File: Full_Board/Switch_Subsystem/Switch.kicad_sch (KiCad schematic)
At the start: 7 parts, among them U7 JS102011SCQN, U8 UCLAMP3301H.TCT

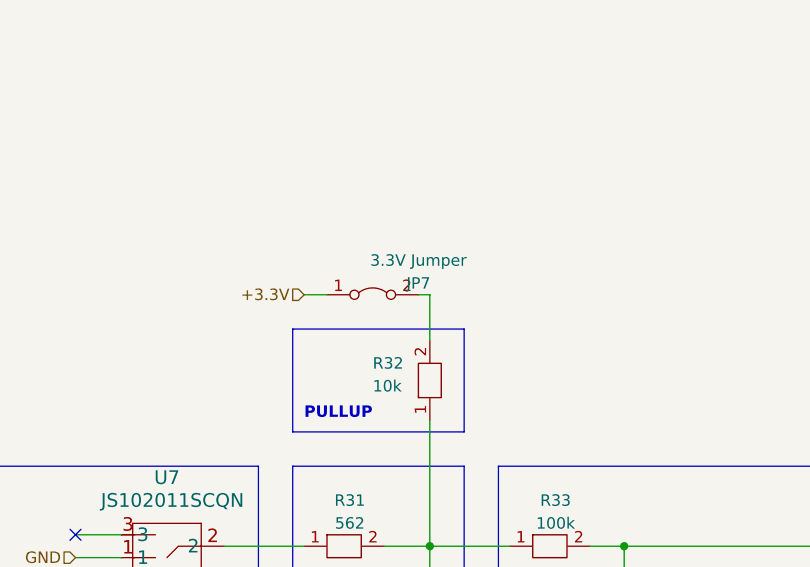
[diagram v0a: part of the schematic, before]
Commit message: Cleanup all schematics and project libs
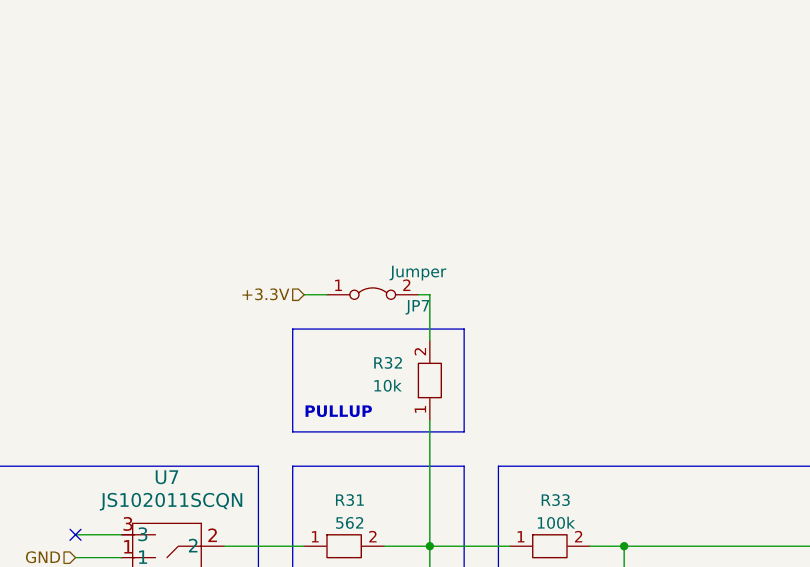
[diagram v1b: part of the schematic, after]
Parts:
- C17: Digikey Link (none) -> https://www.digikey.com/en/products/detail/kemet/C1210C822K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; Digikey link https://www.digikey.com/en/products/detail/kemet/C1210C822K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 -> (none); Mouser Link (none) -> https://www.mouser.com/ProductDetail/KEMET/C1210C822K2RACAU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; Mouser link https://www.mouser.com/ProductDetail/KEMET/C1210C822K2RACAU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 -> (none)
- JP7: value 3.3V Jumper -> Jumper; symbol Jumper:Jumper_2_Bridged -> PH1-02-UA:PH1-02-UA; Digikey Link https://www.digikey.com/en/products/detail/adam-tech/PH1-02-UA/9830266 -> https://www.digikey.com/en/products/detail/adam-tech/PH1-02-UA/9830266?s=N4IgTCBcDa4AwFYDsBaACgCQIwrmFAqgIIoByAIiALoC%2BQA; Manufacturer's Part Number (none) -> PH1-02-UA; Manufacturers Part Number PH1-02-UA -> (none)
- R31: Digikey Link (none) -> https://www.digikey.com/en/products/detail/bourns-inc/CR040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; Digikey link https://www.digikey.com/en/products/detail/bourns-inc/CR040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 -> (none); Mouse link https://www.mouser.com/ProductDetail/Bourns/CR0402-FX-5620G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 -> (none); Mouser Link (none) -> https://www.mouser.com/ProductDetail/Bourns/CR0402-FX-5620G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
- R32: Digikey Link (none) -> https://www.digikey.com/en/products/detail/stackpole-electr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; Digikey link https://www.digikey.com/en/products/detail/stackpole-electr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 -> (none)
- R33: Digikey Link (none) -> https://www.digikey.com/en/products/detail/vishay-dale/RCV2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; Digikey link https://www.digikey.com/en/products/detail/vishay-dale/RCV2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 -> (none); Mouser Link (none) -> https://www.mouser.com/ProductDetail/Vishay-Draloric/RCV251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; Mouser link https://www.mouser.com/ProductDetail/Vishay-Draloric/RCV251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 -> (none)
- U7: Digikey Link (none) -> https://www.digikey.com/en/products/detail/c-k/JS102011SCQN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; Digikey link https://www.digikey.com/en/products/detail/c-k/JS102011SCQN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 -> (none); Mouser Link (none) -> https://www.mouser.com/ProductDetail/CK/JS102011SCQN?qs=aIx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; Mouser link https://www.mouser.com/ProductDetail/CK/JS102011SCQN?qs=aIx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 -> (none)
- U8: Manufacturer's Part Number (none) -> UCLAMP3301H.TCT; Manufacturers Part Number UCLAMP3301H.TCT -> (none); Mouser Link (none) -> https://www.mouser.com/ProductDetail/Semtech/UCLAMP3301H.TC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; Mouser Part Number (none) -> 947-UCLAMP3301H.TCT
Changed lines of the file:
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@@
       (effects (font (size 1.27 1.27)) (justify left) hide)
     )
-    (property "Digikey link" "https://www.digikey.com/en/products/detail/stackpole-electronics-inc/RMCF1206FT10K0/1759669" (id 7) (at 148.59 66.04 0)
+    (property "Digikey Link" "https://www.digikey.com/en/products/detail/stackpole-electronics-inc/RMCF1206FT10K0/1759669" (id 7) (at 148.59 66.04 0)
       (effects (font (size 1.27 1.27)) (justify left) hide)
     )
-    (property "Mouser link" "" (id 8) (at 151.13 66.04 0)
+    (property "Mouser Link" "" (id 8) (at 151.13 66.04 0)
       (effects (font (size 1.27 1.27)) (justify left) hide)
     )
@@
       (effects (font (size 1.27 1.27)) (justify left) hide)
     )
-    (property "Digikey link" "https://www.digikey.com/en/products/detail/kemet/C1210C822K2RACAUTO/16524786?s=N4IgTCBcDaIMIEYwIAxwBxjAaTAJQEE4CBVAFQHkACEAXQF8g" (id 7) (at 148.59 96.52 0)
+    (property "Digikey Link" "https://www.digikey.com/en/products/detail/kemet/C1210C822K2RACAUTO/16524786?s=N4IgTCBcDaIMIEYwIAxwBxjAaTAJQEE4CBVAFQHkACEAXQF8g" (id 7) (at 148.59 96.52 0)
       (effects (font (size 1.27 1.27)) (justify left) hide)
     )
-    (property "Mouser link" "https://www.mouser.com/ProductDetail/KEMET/C1210C822K2RACAUTO?qs=sGAEpiMZZMukHu%252BjC5l7YfRfrXj%2FJXIdfvr9FKYreLc%3D" (id 8) (at 151.13 96.52 0)
+    (property "Mouser Link" "https://www.mouser.com/ProductDetail/KEMET/C1210C822K2RACAUTO?qs=sGAEpiMZZMukHu%252BjC5l7YfRfrXj%2FJXIdfvr9FKYreLc%3D" (id 8) (at 151.13 96.52 0)
       (effects (font (size 1.27 1.27)) (justify left) hide)
     )
@@
       (effects (font (size 1.524 1.524)) hide)
     )
-    (property "Manufacturers Part Number" "UCLAMP3301H.TCT" (id 4) (at 158.75 130.81 0)
-      (effects (font (size 1.27 1.27)) hide)
-    )
     (property "Digikey Part Number" "UCLAMP3301HDKR-ND" (id 5) (at 158.75 130.81 0)
       (effects (font (size 1.27 1.27)) hide)
     )
-    (property "Mouser Part Number" "" (id 6) (at 158.75 130.81 0)
+    (property "Mouser Part Number" " 947-UCLAMP3301H.TCT " (id 6) (at 158.75 130.81 0)
       (effects (font (size 1.27 1.27)) hide)
     )
@@
       (effects (font (size 1.27 1.27)) hide)
     )
-    (property "Mouser Link" "" (id 8) (at 158.75 130.81 0)
+    (property "Mouser Link" "https://www.mouser.com/ProductDetail/Semtech/UCLAMP3301H.TCT?qs=rBWM4%252BvDhIeimYmappCp5Q%3D%3D" (id 8) (at 158.75 130.81 0)
+      (effects (font (size 1.27 1.27)) hide)
+    )
+    (property "Manufacturer's Part Number" "UCLAMP3301H.TCT" (id 9) (at 158.75 130.81 0)
       (effects (font (size 1.27 1.27)) hide)
     )
@@
     (pin "2")
   )
-  (symbol (lib_id "Jumper:Jumper_2_Bridged") (at 130.81 66.04 0) (unit 1)
+  (symbol (lib_id "PH1-02-UA:PH1-02-UA") (at 130.81 68.58 0) (unit 1)
     (in_bom yes) (on_board yes)
-    (property "Reference" "JP7" (id 0) (at 135.89 64.77 0))
-    (property "Value" "3.3V Jumper" (id 1) (at 135.89 62.23 0))
-    (property "Footprint" "TestPoint:TestPoint_2Pads_Pitch2.54mm_Drill0.8mm" (id 2) (at 130.81 66.04 0)
+    (property "Reference" "JP7" (id 0) (at 135.89 67.31 0))
+    (property "Value" "Jumper" (id 1) (at 135.89 63.5 0))
+    (property "Footprint" "TestPoint:TestPoint_2Pads_Pitch2.54mm_Drill0.8mm" (id 2) (at 130.81 68.58 0)
       (effects (font (size 1.27 1.27)) hide)
     )
-    (property "Datasheet" "~" (id 3) (at 130.81 66.04 0)
+    (property "Datasheet" "https://app.adam-tech.com/products/download/data_sheet/201605/ph1-xx-ua-data-sheet.pdf" (id 3) (at 130.81 68.58 0)
       (effects (font (size 1.27 1.27)) hide)
     )
-    (property "Manufacturers Part Number" "PH1-02-UA" (id 4) (at 130.81 66.04 0)
+    (property "Digikey Part Number" "2057-PH1-02-UA-ND" (id 5) (at 130.81 68.58 0)
       (effects (font (size 1.27 1.27)) hide)
     )
-    (property "Digikey Part Number" "2057-PH1-02-UA-ND" (id 5) (at 130.81 66.04 0)
+    (property "Mouser Part Number" "" (id 6) (at 130.81 68.58 0)
       (effects (font (size 1.27 1.27)) hide)
     )
-    (property "Mouser Part Number" "" (id 6) (at 130.81 66.04 0)
+    (property "Digikey Link" "https://www.digikey.com/en/products/detail/adam-tech/PH1-02-UA/9830266?s=N4IgTCBcDa4AwFYDsBaACgCQIwrmFAqgIIoByAIiALoC%2BQA" (id 7) (at 130.81 68.58 0)
       (effects (font (size 1.27 1.27)) hide)
     )
-    (property "Digikey Link" "https://www.digikey.com/en/products/detail/adam-tech/PH1-02-UA/9830266" (id 7) (at 130.81 66.04 0)
+    (property "Mouser Link" "" (id 8) (at 130.81 68.58 0)
       (effects (font (size 1.27 1.27)) hide)
     )
-    (property "Mouser Link" "" (id 8) (at 130.81 66.04 0)
+    (property "Manufacturer's Part Number" "PH1-02-UA" (id 9) (at 130.81 68.58 0)
       (effects (font (size 1.27 1.27)) hide)
     )
@@
       (effects (font (size 1.27 1.27)) (justify left) hide)
     )
-    (property "Digikey link" "https://www.digikey.com/en/products/detail/bourns-inc/CR0402-FX-5620GLF/3783429?s=N4IgTCBcDaIAQGEBKAGALCsBaAYgDSwFYA2MFAcQBkcQBdAXyA" (id 7) (at 137.16 105.41 0)
+    (property "Digikey Link" "https://www.digikey.com/en/products/detail/bourns-inc/CR0402-FX-5620GLF/3783429?s=N4IgTCBcDaIAQGEBKAGALCsBaAYgDSwFYA2MFAcQBkcQBdAXyA" (id 7) (at 137.16 105.41 0)
       (effects (font (size 1.27 1.27)) (justify left) hide)
     )
-    (property "Mouse link" "https://www.mouser.com/ProductDetail/Bourns/CR0402-FX-5620GLF?qs=sGAEpiMZZMtlubZbdhIBIDfFWzqdPB9%252B4rUQL12%252Bb9s%3D" (id 8) (at 137.16 107.95 0)
+    (property "Mouser Link" "https://www.mouser.com/ProductDetail/Bourns/CR0402-FX-5620GLF?qs=sGAEpiMZZMtlubZbdhIBIDfFWzqdPB9%252B4rUQL12%252Bb9s%3D" (id 8) (at 137.16 107.95 0)
       (effects (font (size 1.27 1.27)) (justify left) hide)
     )
@@
       (effects (font (size 1.27 1.27)) (justify left) hide)
     )
-    (property "Digikey link" "https://www.digikey.com/en/products/detail/vishay-dale/RCV2512100KFKEGAT/13985179?s=N4IgTCBcDaIEoGEBqYCsBGM6AM2DSAYngKIDiAggCoAEIAugL5A" (id 7) (at 160.02 107.95 0)
+    (property "Digikey Link" "https://www.digikey.com/en/products/detail/vishay-dale/RCV2512100KFKEGAT/13985179?s=N4IgTCBcDaIEoGEBqYCsBGM6AM2DSAYngKIDiAggCoAEIAugL5A" (id 7) (at 160.02 107.95 0)
       (effects (font (size 1.27 1.27)) (justify left) hide)
     )
-    (property "Mouser link" "https://www.mouser.com/ProductDetail/Vishay-Draloric/RCV2512100KFKEGAT?qs=sGAEpiMZZMtlubZbdhIBIOK8YY79HZuiqCZ6uF64pjM%3D" (id 8) (at 160.02 105.41 0)
+    (property "Mouser Link" "https://www.mouser.com/ProductDetail/Vishay-Draloric/RCV2512100KFKEGAT?qs=sGAEpiMZZMtlubZbdhIBIOK8YY79HZuiqCZ6uF64pjM%3D" (id 8) (at 160.02 105.41 0)
       (effects (font (size 1.27 1.27)) (justify left) hide)
     )
@@
       (effects (font (size 1.27 1.27)) hide)
     )
-    (property "Digikey link" "https://www.digikey.com/en/products/detail/c-k/JS102011SCQN/3753547" (id 7) (at 114.3 91.44 0)
+    (property "Digikey Link" "https://www.digikey.com/en/products/detail/c-k/JS102011SCQN/3753547" (id 7) (at 114.3 91.44 0)
       (effects (font (size 1.27 1.27)) hide)
     )
-    (property "Mouser link" "https://www.mouser.com/ProductDetail/CK/JS102011SCQN?qs=aIxPIZZxLh/C/w7UJtfwsg%3D%3D" (id 8) (at 114.3 91.44 0)
+    (property "Mouser Link" "https://www.mouser.com/ProductDetail/CK/JS102011SCQN?qs=aIxPIZZxLh/C/w7UJtfwsg%3D%3D" (id 8) (at 114.3 91.44 0)
       (effects (font (size 1.27 1.27)) hide)
     )
